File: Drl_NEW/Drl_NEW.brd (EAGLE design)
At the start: 40.3 x 40.3 mm, 23 parts, among them IC1 TINY13-20SSU, IC2 78L05, Q1 IRF7240PBF, Q2 IRF7240PBF, X1 PROG-ISP6POGOPIN

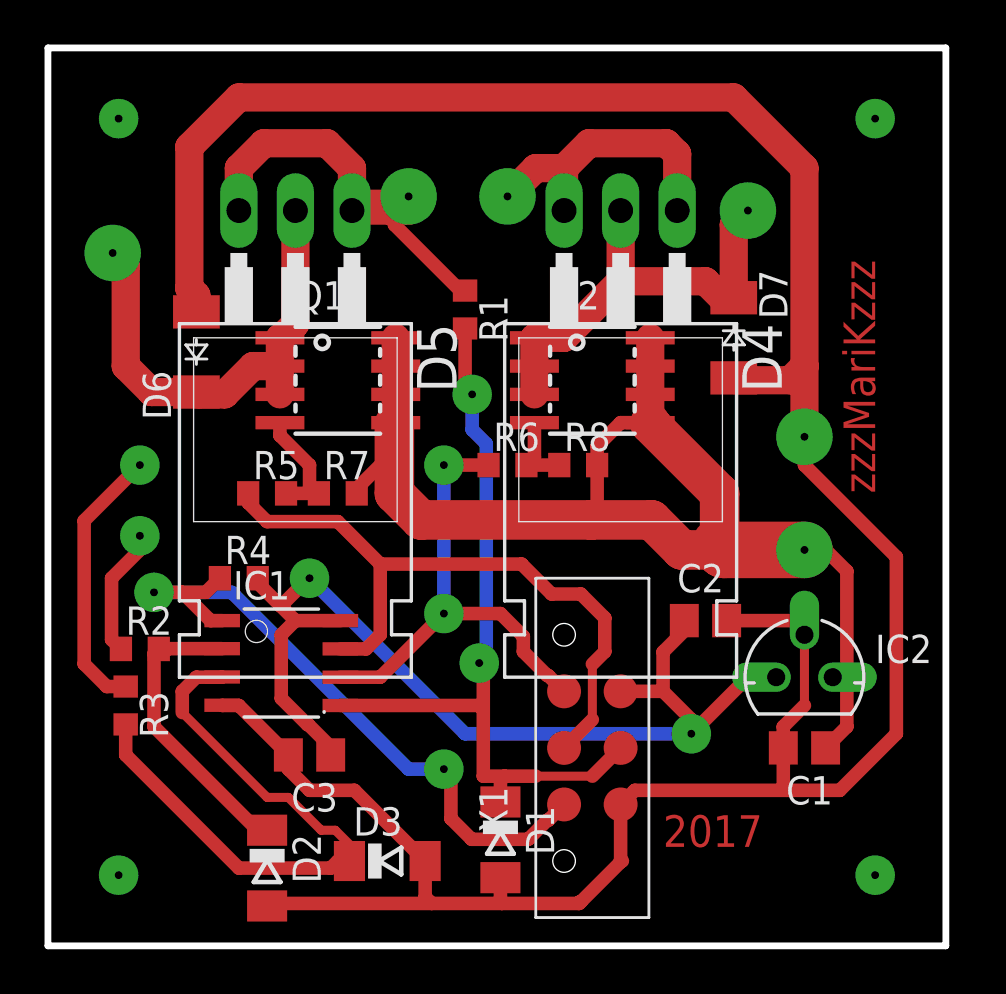
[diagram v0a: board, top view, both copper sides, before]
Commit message: Добавлены ДХО работающие на ШИМ
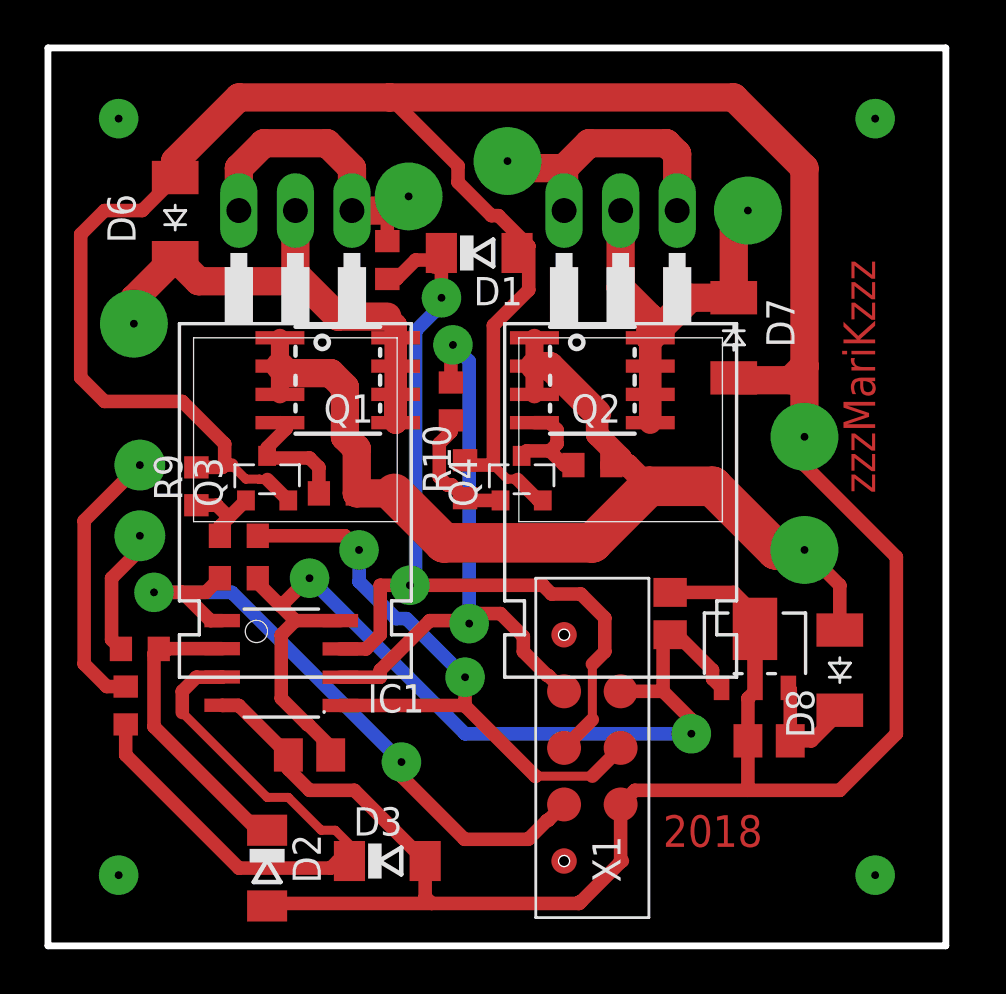
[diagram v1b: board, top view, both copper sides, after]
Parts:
- added D8: MBR0540, diode:SOD-123_MINI-SMA
- added Q3, Q4: SI2302, usb:SOT-23-GSD
- added R10, R9: 10k, rcl:R0603
- IC2: device usb:78LXX -> usb:78LXX-SOT89
- R5, R6: value 47r -> 4r7
- R7, R8: value 47k -> 1k
- moved D1 26.4 mm to (19.4, 31.1), turned to 0 degrees
- moved D6 6.11 mm to (5.71, 32.7)
- moved R1 4.14 mm to (15.2, 30.8)
- moved R6 3.82 mm to (18.1, 24.4), turned to 270 degrees
- moved IC2 2.56 mm to (31.8, 13.3)
- moved R5 2.29 mm to (8.57, 18.4), turned to 180 degrees
- moved C1 1.62 mm to (32.4, 9.21)
- moved C2 1.62 mm to (27.9, 14.9), turned to 90 degrees
- moved R8 0.64 mm to (24.4, 21.6)
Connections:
- new net N$11: Q3.G, R5.2, R9.1
- new net N$12: Q4.G, R10.1, R6.2
- new net N$13: D1.C, IC1.7, R1.2, X1.3
- net +12V: now also D8.A, Q1.1, Q1.2, Q1.3, Q2.1, Q2.2, Q2.3; no longer C1.1, IC2.IN, Q1.5, Q1.6, Q1.7, Q1.8, Q2.5, Q2.6, Q2.7, Q2.8
- net GND: now also IC2.GND@0, IC2.GND@1, Q3.S, Q4.S, R10.2, R9.2; no longer IC2.GND
- net N$4: now also Q4.D; no longer R6.2
- net N$6: now also C1.1, D8.C, IC2.IN; no longer D1.C, IC1.5, R1.2, X1.4
- net N$8: now also Q3.D; no longer R5.2
- net OUT_L: now also IC1.5, X1.4; no longer IC1.7, X1.3
- net PWM_L: now also Q1.5, Q1.6, Q1.7, Q1.8; no longer Q1.1, Q1.2, Q1.3
- net PWM_R: now also Q2.5, Q2.6, Q2.7, Q2.8; no longer Q2.1, Q2.2, Q2.3
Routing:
- net GND: track 129.1 -> 172.6 mm
- net N$13: track 0.00 -> 40.7 mm, vias 0 -> 2
- net N$6: track 35.1 -> 5.27 mm, vias 2 -> 0
- net +12V: track 59.2 -> 49.7 mm
- net DALN_L: track 20.9 -> 14.1 mm
- net OUT_R: track 21.8 -> 27.9 mm
- net N$12: track 0.00 -> 5.95 mm
- net N$11: track 0.00 -> 3.76 mm
- net +5V: track 46.6 -> 44.2 mm
- net OUT_L: track 30.4 -> 28.5 mm, vias 0 -> 2
- net PWM_R: track 20.3 -> 18.9 mm
- net N$4: track 3.53 -> 4.91 mm
- net PWM_L: track 22.6 -> 23.7 mm
- net N$3: track 30.3 -> 29.6 mm
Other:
- board text added: "2018"
- board text removed: "2017"
